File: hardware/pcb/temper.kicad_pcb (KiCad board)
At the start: 2 copper layers, 111.3 x 90 mm, 48 parts, among them J2 nice_view, SW1 SW_PUSH, SW10 SW_PUSH, SW11 SW_PUSH, SW12 SW_PUSH, SW13 SW_PUSH, SW14 SW_PUSH, SW15 SW_PUSH, SW16 SW_PUSH, SW17 SW_PUSH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

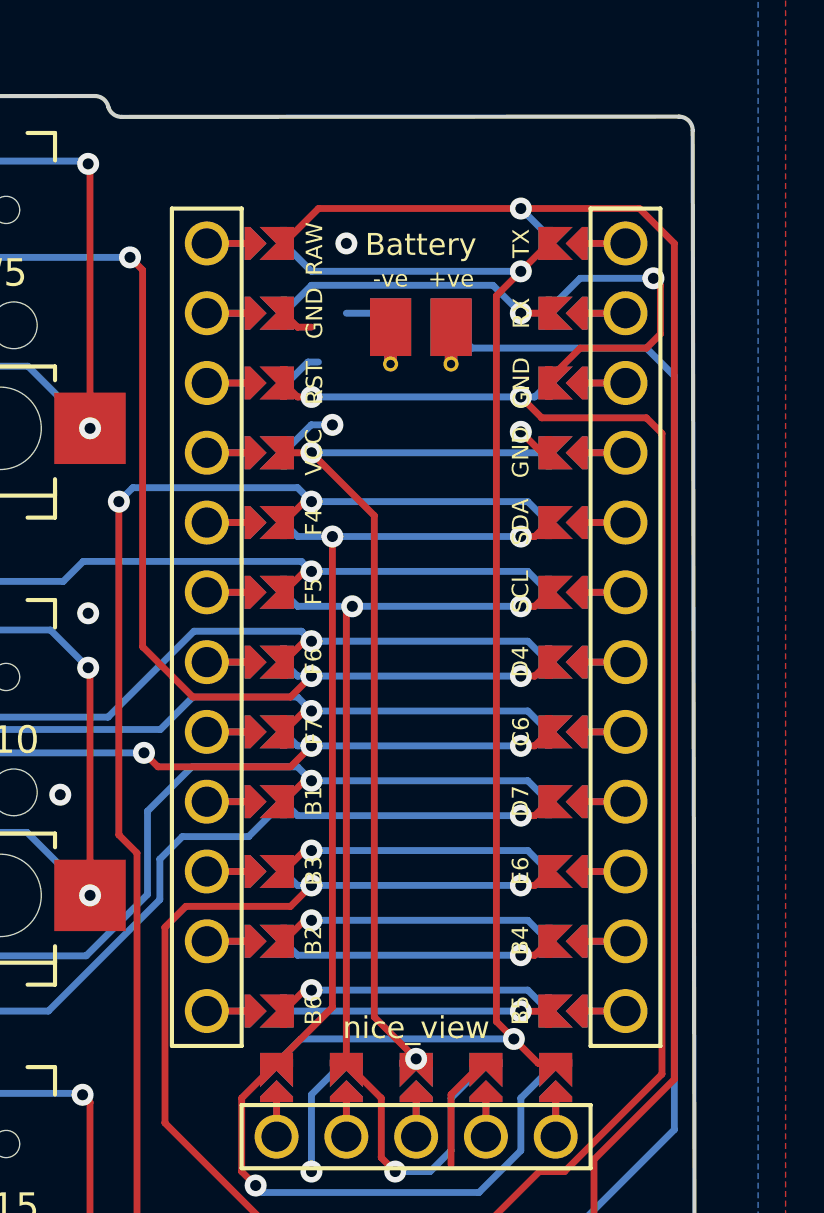
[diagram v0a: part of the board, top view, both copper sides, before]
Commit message: fix: add nice!nano and nice!view silkscreen
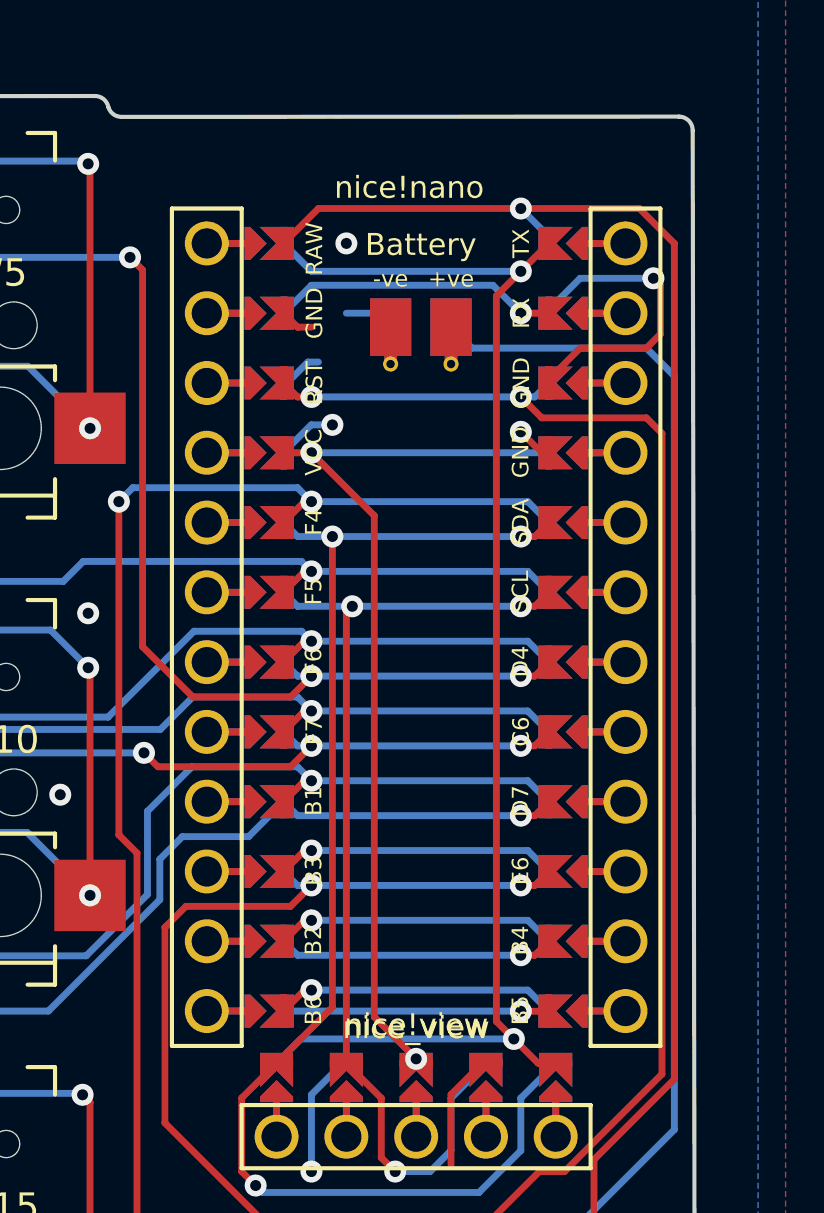
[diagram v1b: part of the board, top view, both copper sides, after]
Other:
- board text added: "nice!nano"
- board text added: "nice!view"
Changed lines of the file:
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@@
     (fp_arc (start -2.5 6.2) (mid -2.146447 6.346447) (end -2 6.7)
       (stroke (width 0.15) (type solid)) (layer "B.SilkS"))
-    (fp_arc (start -1 3.7) (mid -2.06066 3.26066) (end -2.5 2.2)
+    (fp_arc (start -1 3.7) (mid -2.06066 3.260659) (end -2.5 2.2)
       (stroke (width 0.15) (type solid)) (layer "B.SilkS"))
     (fp_line (start -7 -7) (end -6 -7)
@@
     (fp_arc (start -2.5 6.2) (mid -2.146447 6.346447) (end -2 6.7)
       (stroke (width 0.15) (type solid)) (layer "B.Fab"))
-    (fp_arc (start -1 3.7) (mid -2.06066 3.26066) (end -2.5 2.2)
+    (fp_arc (start -1 3.7) (mid -2.06066 3.260659) (end -2.5 2.2)
       (stroke (width 0.15) (type solid)) (layer "B.Fab"))
     (fp_line (start -7.5 -7.5) (end 7.5 -7.5)
@@
     (effects (font (size 1.5 1.5) (thickness 0.3)) (justify left mirror))
   )
+  (gr_text "nice!view" (at 178.054 86.868) (layer "B.SilkS")
+    (effects (font (size 0.8 0.8) (thickness 0.1)) (justify mirror))
+  )
+  (gr_text "nice!nano" (at 177.8 56.388) (layer "B.SilkS")
+    (effects (font (size 0.8 0.8) (thickness 0.1)) (justify mirror))
+  )
   (gr_text "temper\n@raeedcho" (at 127.12 98.75) (layer "F.SilkS")
     (effects (font (size 1.5 1.5) (thickness 0.3)) (justify right))
   )
+  (gr_text "nice!view" (at 178.054 86.868) (layer "F.SilkS")
+    (effects (font (size 0.8 0.8) (thickness 0.1)))
+  )
+  (gr_text "nice!nano" (at 177.8 56.388) (layer "F.SilkS")
+    (effects (font (size 0.8 0.8) (thickness 0.1)))
+  )
   (segment (start 96.52 53.6448) (end 97.8916 52.2732) (width 0.25) (layer "F.Cu") (net 1))
